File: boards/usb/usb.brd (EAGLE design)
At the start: 15.4 x 17.3 mm, 3 parts

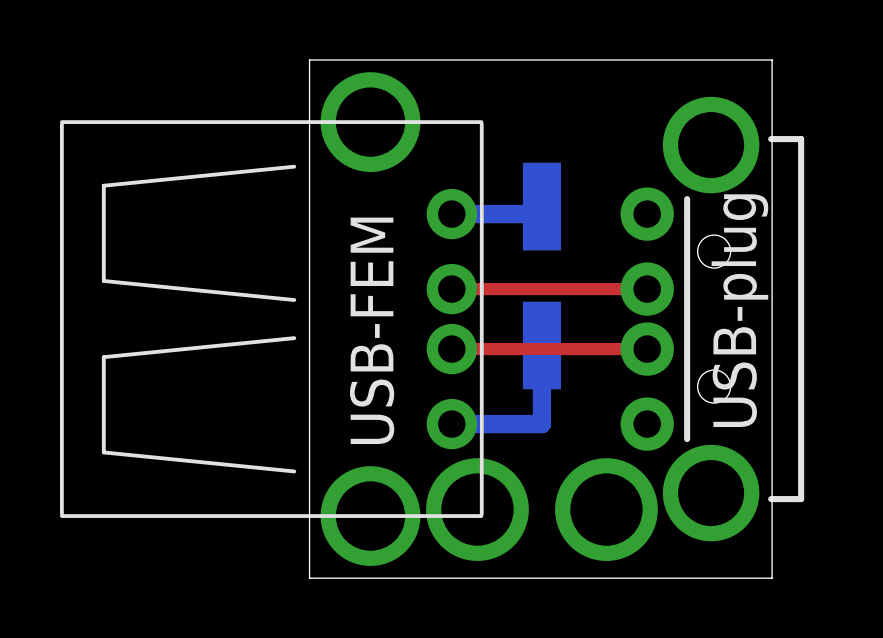
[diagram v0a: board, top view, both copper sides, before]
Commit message: Minor tweaks to USB board: wider, silkscreen
- wider so male USB can be moved in for better support
- added version stamp and tweaked other silk
- labeled signal lines in schematic
- added dimension layer to top silk in CAM job
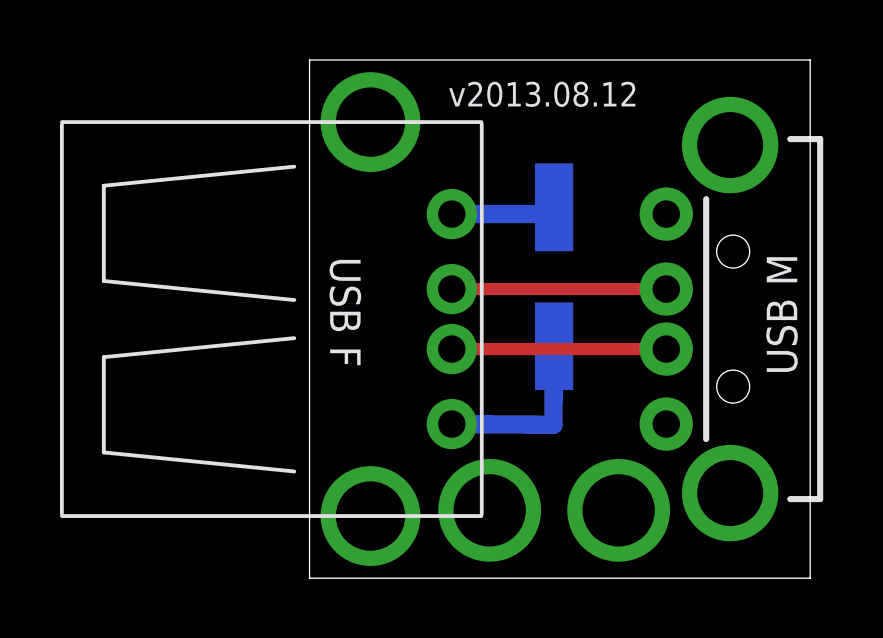
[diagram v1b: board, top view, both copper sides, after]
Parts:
- moved U$2 0.63 mm to (14.0, 8.64)
- moved X3 0.41 mm to (8.15, 2.26)
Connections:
- net N$3 renamed D+
- net N$4 renamed D-
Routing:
- net D-: track 6.51 -> 7.15 mm
- net D+: track 6.51 -> 7.15 mm
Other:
- board size 15.4 x 17.3 mm -> 16.7 x 17.3 mm
- board text added: "USB F"
- board text added: "USB M"
- board text added: "v2013.08.12"
- board text removed: "USB-FEM"
- board text removed: "USB-plug"
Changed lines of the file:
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@@
 <board>
 <plain>
-<wire x1="0" y1="0" x2="15.4178" y2="0" width="0" layer="20"/>
-<wire x1="15.4178" y1="0" x2="15.4178" y2="17.272" width="0" layer="20"/>
-<wire x1="15.4178" y1="17.272" x2="0" y2="17.272" width="0" layer="20"/>
+<wire x1="0" y1="0" x2="16.6878" y2="0" width="0" layer="20"/>
+<wire x1="16.6878" y1="0" x2="16.6878" y2="17.272" width="0" layer="20"/>
+<wire x1="16.6878" y1="17.272" x2="0" y2="17.272" width="0" layer="20"/>
 <wire x1="0" y1="17.272" x2="0" y2="0" width="0" layer="20"/>
-<text x="2.794" y="4.318" size="1.4224" layer="121" rot="R90">USB-FEM</text>
-<text x="13.462" y="12.954" size="1.4224" layer="121" rot="R270">USB-plug</text>
+<text x="0.6858" y="10.7188" size="1.016" layer="121" rot="SR270">USB F</text>
+<text x="15.24" y="10.8204" size="1.016" layer="121" rot="R270">USB M</text>
+<text x="4.6228" y="15.7226" size="0.8128" layer="121" font="vector">v2013.08.12</text>
 </plain>
 <attributes>
@@
 </autorouter>
 <elements>
-<element name="X3" library="con-molex-micro-fit-3_0" package="43045-0206" value="" x="7.747" y="2.286" smashed="yes" rot="MR0"/>
+<element name="X3" library="con-molex-micro-fit-3_0" package="43045-0206" value="" x="8.1534" y="2.2606" smashed="yes" rot="MR0"/>
 <element name="U$1" library="ngohara_parts" package="USB-A-S" value="USB-A_FEM" x="2.032" y="8.636" smashed="yes"/>
-<element name="U$2" library="ngohara_parts" package="USB-A-H" value="USB-A-PLUG" x="13.3858" y="8.636" smashed="yes" rot="R180"/>
+<element name="U$2" library="ngohara_parts" package="USB-A-H" value="USB-A-PLUG" x="14.0208" y="8.636" smashed="yes" rot="R180"/>
 </elements>
 <signals>
@@
 <signal name="N$2">
 </signal>
-<signal name="N$3">
+<signal name="D+">
 <contactref element="U$1" pad="D+"/>
 <contactref element="U$2" pad="D+"/>
-<wire x1="4.742" y1="7.636" x2="11.2558" y2="7.636" width="0.4064" layer="1"/>
-</signal>
-<signal name="N$4">
+<wire x1="4.742" y1="7.636" x2="11.8908" y2="7.636" width="0.4064" layer="1"/>
+</signal>
+<signal name="D-">
 <contactref element="U$2" pad="D-"/>
 <contactref element="U$1" pad="D-"/>
-<wire x1="4.742" y1="9.636" x2="11.2558" y2="9.636" width="0.4064" layer="1"/>
+<wire x1="4.742" y1="9.636" x2="11.8908" y2="9.636" width="0.4064" layer="1"/>
 </signal>
 <signal name="GND" class="1">
 <contactref element="U$1" pad="GND"/>
 <contactref element="X3" pad="P$1"/>
-<wire x1="4.742" y1="5.136" x2="7.747" y2="5.136" width="0.6096" layer="16"/>
-<wire x1="7.747" y1="5.136" x2="7.747" y2="7.756" width="0.6096" layer="16"/>
+<wire x1="4.742" y1="5.136" x2="8.128" y2="5.1106" width="0.6096" layer="16"/>
+<wire x1="8.128" y1="5.1106" x2="8.1534" y2="7.7306" width="0.6096" layer="16"/>
 </signal>
 <signal name="VCC" class="1">
@@
 <contactref element="U$1" pad="VCC"/>
 <wire x1="4.742" y1="12.136" x2="7.7724" y2="12.136" width="0.6096" layer="16"/>
-<wire x1="7.7724" y1="12.136" x2="7.747" y2="12.386" width="0.6096" layer="16"/>
+<wire x1="7.7724" y1="12.136" x2="8.1534" y2="12.3606" width="0.6096" layer="16"/>
 </signal>
 </signals>
